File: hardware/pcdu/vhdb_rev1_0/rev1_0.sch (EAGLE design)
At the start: 64 parts, among them J1 AJP92A8813, J2 AJP92A8813, J3 AJP92A8813, J4 AJP92A8813, J5 AJP92A8813, Q1 25MHz, SW1 KSZ9897RTXC

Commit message: Added lan transformers
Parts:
- removed C35, C36, C37, C38, C39, C40, C41, C42, C43, C44, C45, C46, C47, C48: (no value), rcl:C-EUC0805
- removed PHY1: KSZ9031RNX, KSZ9031RNX:KSZ9031RNX
- removed R3: 12.1 kΩ, resistor:R-EU_R0805
- removed R4, R5, R6, R7: 10K, resistor:R-EU_R0805
- added C49, C50, C51, C52, C53, C54, C55, C56, C57, C58, C59, C60, C61, C62: (no value), rcl:C-EUC0805
- added MAG1, MAG2, MAG3, MAG4, MAG5: 749020010A, 749023010A:749020010A
- added PHY2: KSZ9031RNX, KSZ9031RNX:KSZ9031RNX
- added R10, R11, R12, R9: 10K, resistor:R-EU_R0805
- added R8: 12.1 kΩ, resistor:R-EU_R0805
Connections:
- removed net N$10: PHY1.TX_EN, SW1.TX_EN7/TX_CTL7
- removed net N$11: PHY1.GTX_CLK, SW1.TX_CLK7/REFCLKI7
- removed net N$12: PHY1.RX_DV/CLK125_EN, SW1.RX_DV7/CRS_DV7/RX_CTL7
- removed net N$13: PHY1.RX_CLK/PHYAD2, SW1.RX_CLK7/REFCLKO7
- removed net N$15: PHY1.ISET, R3.2
- removed net N$6: PHY1.TXD0, SW1.RXD7_0
- removed net N$7: PHY1.TXD1, SW1.RXD7_1
- removed net N$8: PHY1.TXD2, SW1.RXD7_2
- removed net N$9: PHY1.TXD3, SW1.RXD7_3
- new net D54_N: MAG5.TD4-, SW1.TXRX5M_D
- new net D54_P: MAG5.TD4+, SW1.TXRX5P_D
- new net N$1: MAG1.TD1+, SW1.TXRX1P_A
- new net N$100: PHY2.ISET, R8.2
- new net N$16: MAG1.TD3+, SW1.TXRX1P_C
- new net N$17: MAG1.TD3-, SW1.TXRX1M_C
- new net N$18: MAG1.TD4+, SW1.TXRX1P_D
- new net N$19: MAG1.TD4-, SW1.TXRX1M_D
- new net N$20: MAG2.TD1+, SW1.TXRX2P_A
- new net N$21: MAG2.TD1-, SW1.TXRX2M_A
- new net N$22: MAG2.TD2+, SW1.TXRX2P_B
- new net N$23: MAG2.TD2-, SW1.TXRX2M_B
- new net N$24: MAG2.TD3+, SW1.TXRX2P_C
- new net N$25: MAG2.TD3-, SW1.TXRX2M_C
- new net N$26: MAG2.TD4+, SW1.TXRX2P_D
- new net N$27: MAG2.TD4-, SW1.TXRX2M_D
- new net N$28: MAG3.TD1+, SW1.TXRX3P_A
- new net N$29: MAG3.TD1-, SW1.TXRX3M_A
- new net N$3: MAG1.TD1-, SW1.TXRX1M_A
- new net N$30: MAG3.TD2+, SW1.TXRX3P_B
- new net N$31: MAG3.TD2-, SW1.TXRX3M_B
- new net N$32: MAG3.TD3+, SW1.TXRX3P_C
- new net N$33: MAG3.TD3-, SW1.TXRX3M_C
- new net N$34: MAG3.TD4+, SW1.TXRX3P_D
- new net N$35: MAG3.TD4-, SW1.TXRX3M_D
- new net N$38: MAG5.TD3-, SW1.TXRX5M_C
- new net N$39: MAG5.TD3+, SW1.TXRX5P_C
- new net N$4: MAG1.TD2+, SW1.TXRX1P_B
- new net N$40: MAG5.TD2-, SW1.TXRX5M_B
- new net N$41: MAG5.TD2+, SW1.TXRX5P_B
- new net N$42: MAG5.TD1-, SW1.TXRX5M_A
- new net N$43: MAG5.TD1+, SW1.TXRX5P_A
- new net N$44: MAG4.TD4-, SW1.TXRX4M_D
- new net N$45: MAG4.TD4+, SW1.TXRX4P_D
- new net N$46: MAG4.TD3-, SW1.TXRX4M_C
- new net N$47: MAG4.TD3+, SW1.TXRX4P_C
- new net N$48: MAG4.TD2-, SW1.TXRX4M_B
- new net N$49: MAG4.TD2+, SW1.TXRX4P_B
- new net N$5: MAG1.TD2-, SW1.TXRX1M_B
- new net N$50: MAG4.TD1-, SW1.TXRX4M_A
- new net N$51: MAG4.TD1+, SW1.TXRX4P_A
- new net N$52: J1.A+, MAG1.MX1+
- new net N$53: J1.A-, MAG1.MX1-
- new net N$54: J1.B+, MAG1.MX2+
- new net N$55: J1.B-, MAG1.MX2-
- new net N$56: J1.C+, MAG1.MX3+
- new net N$57: J1.C-, MAG1.MX3-
- new net N$58: J1.D+, MAG1.MX4+
- new net N$59: J1.D-, MAG1.MX4-
- new net N$60: J2.A+, MAG2.MX1+
- new net N$61: J2.A-, MAG2.MX1-
- new net N$62: J2.B+, MAG2.MX2+
- new net N$63: J2.B-, MAG2.MX2-
- new net N$64: J2.C+, MAG2.MX3+
- new net N$65: J2.C-, MAG2.MX3-
- new net N$66: J2.D+, MAG2.MX4+
- new net N$67: J2.D-, MAG2.MX4-
- new net N$68: J3.A+, MAG3.MX1+
- new net N$69: J3.A-, MAG3.MX1-
- new net N$70: J3.B+, MAG3.MX2+
- new net N$71: J3.B-, MAG3.MX2-
- new net N$72: J3.C+, MAG3.MX3+
- new net N$73: J3.C-, MAG3.MX3-
- new net N$74: J3.D+, MAG3.MX4+
- new net N$75: J3.D-, MAG3.MX4-
- new net N$76: J4.A+, MAG4.MX1+
- new net N$77: J4.A-, MAG4.MX1-
- new net N$78: J4.B+, MAG4.MX2+
- new net N$79: J4.B-, MAG4.MX2-
- new net N$80: J4.C+, MAG4.MX3+
- new net N$81: J4.C-, MAG4.MX3-
- new net N$82: J4.D+, MAG4.MX4+
- new net N$83: J4.D-, MAG4.MX4-
- new net N$84: J5.A+, MAG5.MX1+
- new net N$85: J5.A-, MAG5.MX1-
- new net N$86: J5.B+, MAG5.MX2+
- new net N$87: J5.B-, MAG5.MX2-
- new net N$88: J5.C+, MAG5.MX3+
- new net N$89: J5.C-, MAG5.MX3-
- new net N$90: J5.D+, MAG5.MX4+
- new net N$91: J5.D-, MAG5.MX4-
- new net N$92: PHY2.TXD0, SW1.RXD6_0
- new net N$93: PHY2.TXD1, SW1.RXD6_1
- new net N$94: PHY2.TXD2, SW1.RXD6_2
- new net N$95: PHY2.TXD3, SW1.RXD6_3
- new net N$96: PHY2.RX_DV/CLK125_EN, SW1.RX_DV6/CRS_DV6/RX_CTL6
- new net N$97: PHY2.RX_CLK/PHYAD2, SW1.RX_CLK6/REFCLKO6
- new net N$98: PHY2.TX_EN, SW1.TX_EN6/TX_CTL6
- new net N$99: PHY2.GTX_CLK, SW1.TX_CLK6/REFCLKI6
- net AVDDH: now also PHY2.AVDDH@1, PHY2.AVDDH@2; no longer PHY1.AVDDH@1, PHY1.AVDDH@2
- net AVDDL: now also PHY2.AVDDL@1, PHY2.AVDDL@2, PHY2.AVDDL_PLL; no longer PHY1.AVDDL@1, PHY1.AVDDL@2, PHY1.AVDDL_PLL
- net DVDDL: now also C49.1, PHY2.DVDDL@1, PHY2.DVDDL@2, PHY2.DVDDL@3, PHY2.DVDDL@4, PHY2.DVDDL@5, PHY2.DVDDL@6; no longer C35.1, PHY1.DVDDL@1, PHY1.DVDDL@2, PHY1.DVDDL@3, PHY1.DVDDL@4, PHY1.DVDDL@5, PHY1.DVDDL@6
- net GND: now also C49.2, C51.2, C52.2, C53.2, C54.2, C55.2, C57.2, C58.2, C60.2, C61.2, C62.2, PHY2.P_GND, PHY2.VSS, R12.1, R8.1; no longer C35.2, C37.2, C38.2, C39.2, C40.2, C41.2, C43.2, C44.2, C46.2, C47.2, C48.2, PHY1.P_GND, PHY1.VSS, R3.1, R7.1
- net MODE0: now also PHY2.RXD0/MODE0, R12.2, SW1.TXD6_0; no longer PHY1.RXD0/MODE0, R7.2, SW1.TXD7_0
- net MODE1: now also PHY2.RXD1/MODE1, R11.2, SW1.TXD6_1; no longer PHY1.RXD1/MODE1, R6.2
- net MODE2: now also PHY2.RXD2/MODE2, R10.2, SW1.TXD6_2; no longer PHY1.RXD2/MODE2, R5.2
- net MODE3: now also PHY2.RXD3/MODE3, R9.2, SW1.TXD6_3; no longer PHY1.RXD3/MODE3, R4.2, SW1.TXD7_3
- net RESET: now also PHY2.RESET_N; no longer PHY1.RESET_N
- net VDDIO: now also PHY2.DVDDH@1, PHY2.DVDDH@2, PHY2.DVDDH@3, R10.1, R11.1, R9.1; no longer PHY1.DVDDH@1, PHY1.DVDDH@2, PHY1.DVDDH@3, R4.1, R5.1, R6.1
- net XI: now also PHY2.XI; no longer PHY1.XI
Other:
- moved on the sheet: J1, J2, J3, J4, J5

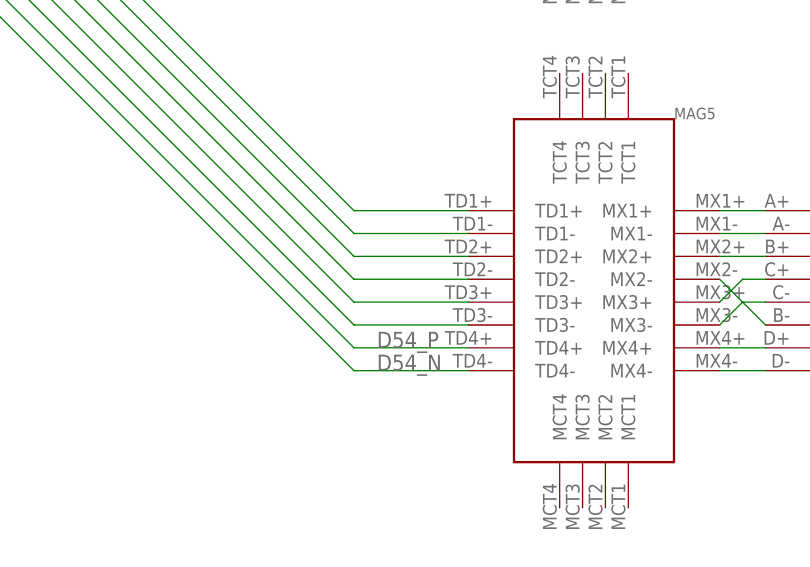
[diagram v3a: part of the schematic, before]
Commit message: Minor changes to high density board
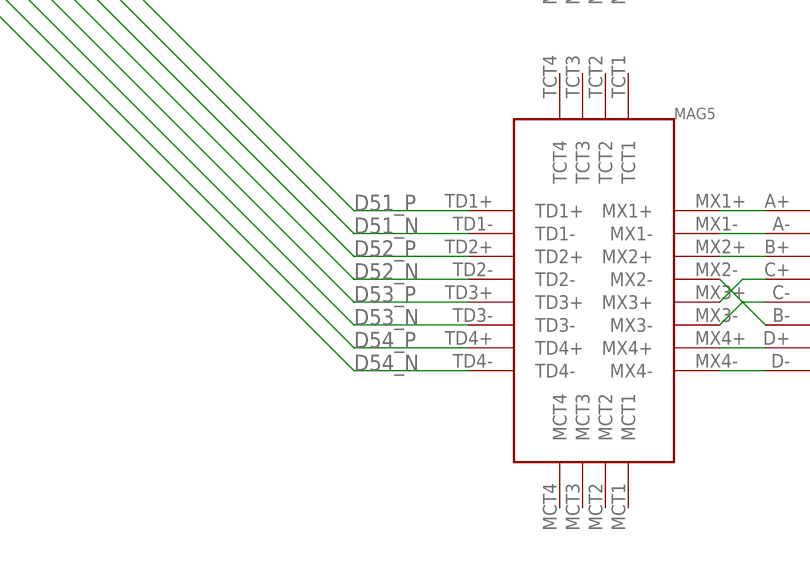
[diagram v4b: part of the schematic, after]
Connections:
- net N$38 renamed D53_N
- net N$39 renamed D53_P
- net N$40 renamed D52_N
- net N$41 renamed D52_P
- net N$42 renamed D51_N
- net N$43 renamed D51_P
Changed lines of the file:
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@@
 <class number="0" name="default" width="0" drill="0">
+</class>
+<class number="1" name="diff" width="0.127" drill="0.3">
+<clearance class="0" value="0.508"/>
+<clearance class="1" value="0.127"/>
 </class>
 </classes>
@@
 </segment>
 </net>
-<net name="D54_N" class="0">
+<net name="D54_N" class="1">
 <segment>
 <pinref part="SW1" gate="G$1" pin="TXRX5M_D"/>
@@
 <wire x1="132.08" y1="-27.94" x2="190.5" y2="-86.36" width="0.1524" layer="91"/>
 <wire x1="190.5" y1="-86.36" x2="203.2" y2="-86.36" width="0.1524" layer="91"/>
-<label x="193.04" y="-86.36" size="1.778" layer="95"/>
-</segment>
-</net>
-<net name="D54_P" class="0">
+<label x="190.5" y="-86.36" size="1.778" layer="95"/>
+</segment>
+</net>
+<net name="D54_P" class="1">
 <segment>
 <pinref part="SW1" gate="G$1" pin="TXRX5P_D"/>
@@
 <wire x1="132.08" y1="-25.4" x2="190.5" y2="-83.82" width="0.1524" layer="91"/>
 <wire x1="190.5" y1="-83.82" x2="203.2" y2="-83.82" width="0.1524" layer="91"/>
-<label x="193.04" y="-83.82" size="1.778" layer="95"/>
-</segment>
-</net>
-<net name="N$38" class="0">
+<label x="190.5" y="-83.82" size="1.778" layer="95"/>
+</segment>
+</net>
+<net name="D53_N" class="1">
 <segment>
 <pinref part="SW1" gate="G$1" pin="TXRX5M_C"/>
@@
 <wire x1="132.08" y1="-22.86" x2="190.5" y2="-81.28" width="0.1524" layer="91"/>
 <wire x1="190.5" y1="-81.28" x2="203.2" y2="-81.28" width="0.1524" layer="91"/>
-</segment>
-</net>
-<net name="N$39" class="0">
+<label x="190.5" y="-81.28" size="1.778" layer="95"/>
+</segment>
+</net>
+<net name="D53_P" class="1">
 <segment>
 <pinref part="SW1" gate="G$1" pin="TXRX5P_C"/>
@@
 <wire x1="132.08" y1="-20.32" x2="190.5" y2="-78.74" width="0.1524" layer="91"/>
 <wire x1="190.5" y1="-78.74" x2="203.2" y2="-78.74" width="0.1524" layer="91"/>
-</segment>
-</net>
-<net name="N$40" class="0">
+<label x="190.5" y="-78.74" size="1.778" layer="95"/>
+</segment>
+</net>
+<net name="D52_N" class="1">
 <segment>
 <pinref part="SW1" gate="G$1" pin="TXRX5M_B"/>
@@
 <wire x1="132.08" y1="-17.78" x2="190.5" y2="-76.2" width="0.1524" layer="91"/>
 <wire x1="190.5" y1="-76.2" x2="203.2" y2="-76.2" width="0.1524" layer="91"/>
-</segment>
-</net>
-<net name="N$41" class="0">
+<label x="190.5" y="-76.2" size="1.778" layer="95"/>
+</segment>
+</net>
+<net name="D52_P" class="1">
 <segment>
 <pinref part="SW1" gate="G$1" pin="TXRX5P_B"/>
@@
 <wire x1="132.08" y1="-15.24" x2="190.5" y2="-73.66" width="0.1524" layer="91"/>
 <wire x1="190.5" y1="-73.66" x2="203.2" y2="-73.66" width="0.1524" layer="91"/>
-</segment>
-</net>
-<net name="N$42" class="0">
+<label x="190.5" y="-73.66" size="1.778" layer="95"/>
+</segment>
+</net>
+<net name="D51_N" class="1">
 <segment>
 <pinref part="SW1" gate="G$1" pin="TXRX5M_A"/>
@@
 <wire x1="132.08" y1="-12.7" x2="190.5" y2="-71.12" width="0.1524" layer="91"/>
 <wire x1="190.5" y1="-71.12" x2="203.2" y2="-71.12" width="0.1524" layer="91"/>
-</segment>
-</net>
-<net name="N$43" class="0">
+<label x="190.5" y="-71.12" size="1.778" layer="95"/>
+</segment>
+</net>
+<net name="D51_P" class="1">
 <segment>
 <pinref part="SW1" gate="G$1" pin="TXRX5P_A"/>
@@
 <wire x1="132.08" y1="-10.16" x2="190.5" y2="-68.58" width="0.1524" layer="91"/>
 <wire x1="190.5" y1="-68.58" x2="203.2" y2="-68.58" width="0.1524" layer="91"/>
-</segment>
-</net>
+<label x="190.5" y="-68.58" size="1.778" layer="95"/>
+</segment>
+</net>
